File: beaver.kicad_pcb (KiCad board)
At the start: 8 copper layers, 31.2 x 44.5 mm, 57 parts, among them J1 Conn_01x04_Male, J2 USB_C_Receptacle_USB2.0, J3 NFC, J4 Conn_01x17, J5 Conn_01x17, SW1 RESET, SW2 USER P0.17, U1 nRF52840, U2 USBLC6-2SC6, U4 AZ1117-3.3, Y1 Crystal_GND24_Small, Y2 Crystal_Small

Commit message: final touches
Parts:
- added C8: 100n, Capacitor_SMD:C_0402_1005Metric, F.Cu at (162.9, 99.0)
- C5, C6, C7: value 1uF -> 100n
- D2: renamed from D5; value YELLOW P0.24 -> Y P0.10
- D3: renamed from D6; value GREEN P0.22 -> G P1.13
- D4: renamed from D7; value RED P0.20 -> R P1.15
- D5: renamed from D3; value POWER -> PWR
- L1: footprint Inductor_SMD:L_0805_2012Metric -> Inductor_SMD:L_0402_1005Metric
- moved C18 15.1 mm to (172.8, 104.2), turned to 90 degrees
- moved J3 13.9 mm to (170.5, 105.2), turned to -90 degrees
- moved L1 11.6 mm to (169.4, 92.2), turned to 180 degrees
- moved C15 11.3 mm to (169.7, 91.3)
- moved C17 10.9 mm to (165.6, 104.3), turned to -90 degrees
- moved D5 3.52 mm to (156.3, 106.6)
- moved C4 2.28 mm to (163.9, 88.0)
- moved R13 1.59 mm to (153.9, 105.8), turned to 180 degrees
- moved J2 1.41 mm to (174.6, 76.1)
- moved AE1 1.18 mm to (170.3, 76.9)
- moved J1 1.15 mm to (149.2, 76.1)
- moved C1 0.95 mm to (168.4, 94.8)
- moved C24 0.76 mm to (169.6, 108.5)
- moved R8 0.76 mm to (168.6, 108.5)
- moved C21 0.71 mm to (169.7, 87.0)
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- renumbered AE2 to AE1, C15 to C1, C18 to C10, C16 to C11, C19 to C12, C20 to C13, C24 to C14, C1 to C15, C2 to C16, C21 to C17, C22 to C18, C25 to C19, C10 to C2, C26 to C20, C3 to C21, C8 to C22, C4 to C23, C23 to C24, C17 to C3, C11 to C4, C27 to C9, J4 to J1, J5 to J2, J2 to J4, J1 to J5, R15 to R10, R5 to R11, R14 to R12, R7 to R13, R17 to R2, R18 to R3, R19 to R4, R2 to R5, R3 to R6, R6 to R7, R13 to R8, R4 to R9, U4 to U1, U1 to U2, U2 to U3, Y2 to Y1, Y1 to Y2
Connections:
- net Net-(AE2-A) renamed /ANT_MATCHED
- net Net-(J1-Pin_2) renamed /SWDCLK
- net Net-(J1-Pin_3) renamed /SWDIO
- net Net-(U1-ANT) renamed /ANT
- Y2 pad 2: unconnected-(Y1-Pad2) -> GNDREF
- Y2 pad 4: unconnected-(Y1-Pad4) -> GNDREF
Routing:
- net /P0.29: track 0.50 -> 26.6 mm, vias 0 -> 1
- net /SWDCLK: track 0.00 -> 20.5 mm, vias 0 -> 1
- net /SWDIO: track 0.00 -> 20.1 mm, vias 0 -> 1
- net /ANT_MATCHED: track 4.36 -> 15.6 mm
- net /ANT: track 13.8 -> 3.30 mm, vias 2 -> 0
- net /NFC-: track 8.88 -> 18.5 mm
- net VDD: track 58.7 -> 49.4 mm, vias 13 -> 14
- net /NFC+: track 8.67 -> 17.6 mm
- net GNDREF: track 20.6 -> 12.5 mm, vias 11 -> 156
- net /USER_BUT: track 18.3 -> 24.6 mm
- net Net-(U2-DEC2): track 4.96 -> 1.86 mm
- net /P1.12: track 25.2 -> 23.2 mm
- net /P0.26: track 12.5 -> 14.1 mm
- net /P0.31: track 17.4 -> 15.9 mm
- net /P0.25: track 14.4 -> 15.9 mm
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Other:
- board text added: "NFC"
- board text added: "R P1.12 G P0.3 B P0.30"
- board text removed: "B P0.30"
- board text removed: "G P0.3"
- board text removed: "R P1.12"

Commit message: fix: rules due to fabric capabilities
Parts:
- moved J2 1.27 mm to (175.8, 76.1)
- moved J1 1.02 mm to (148.1, 76.1)
- moved C12 0.07 mm to (159.2, 99.0)
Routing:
- net /P1.15: track 21.2 -> 18.2 mm
- net /P1.13: track 15.7 -> 13.2 mm
- net /P0.5: track 13.9 -> 15.9 mm
- net /P0.2: track 16.6 -> 18.0 mm
- net /P1.6: track 20.9 -> 22.2 mm
- net /P1.5: track 19.7 -> 20.9 mm
- net /P0.13: track 18.2 -> 19.2 mm
- net /P0.15: track 23.0 -> 24.0 mm
- net /P0.8: track 13.3 -> 14.3 mm
- net /P0.26: track 14.1 -> 15.1 mm
- net /P0.4: track 11.7 -> 12.7 mm
- net /P0.31: track 15.9 -> 16.7 mm
- net GNDREF: track 12.5 -> 13.3 mm, vias 156 -> 128
- net /P0.12: track 17.3 -> 18.0 mm
- net /DEC_4_6: track 12.6 -> 13.2 mm
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
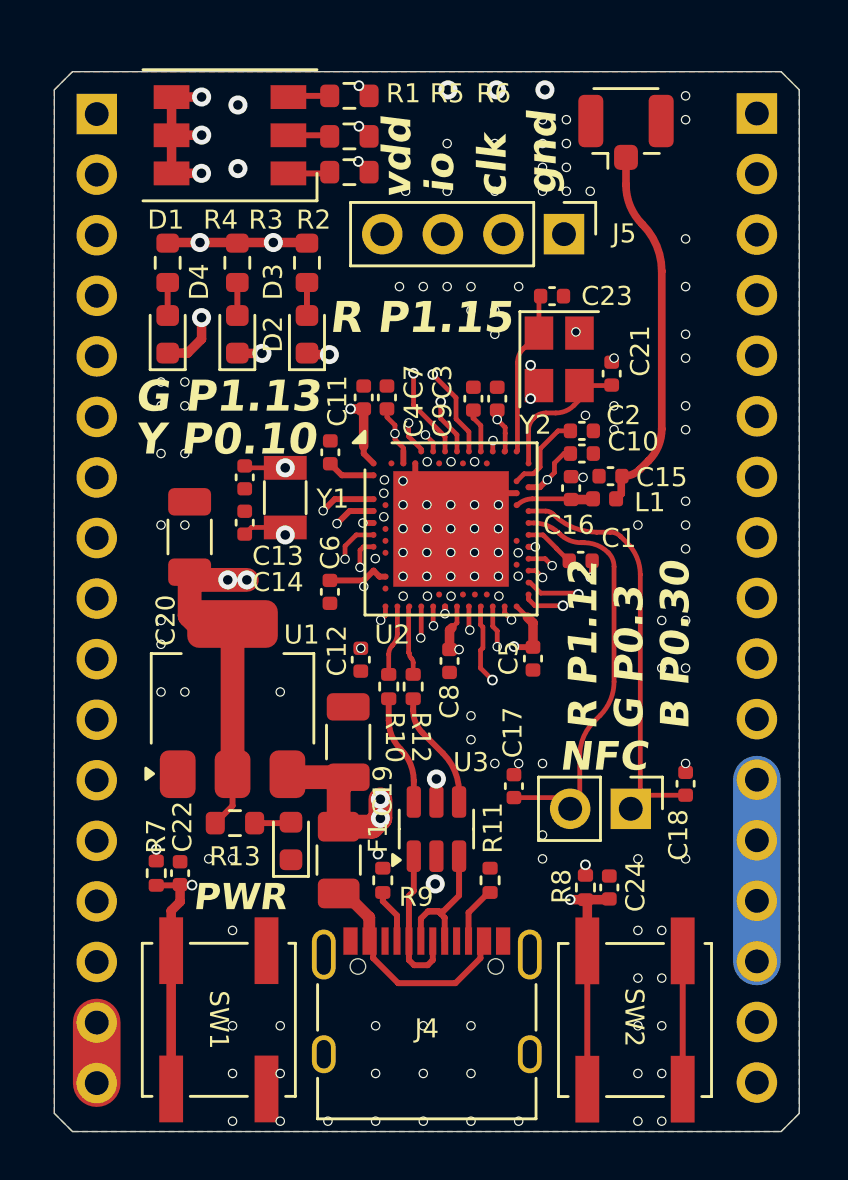
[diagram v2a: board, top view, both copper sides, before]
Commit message: fix: 5V line connection, cat image, text placements, headers edge distanse
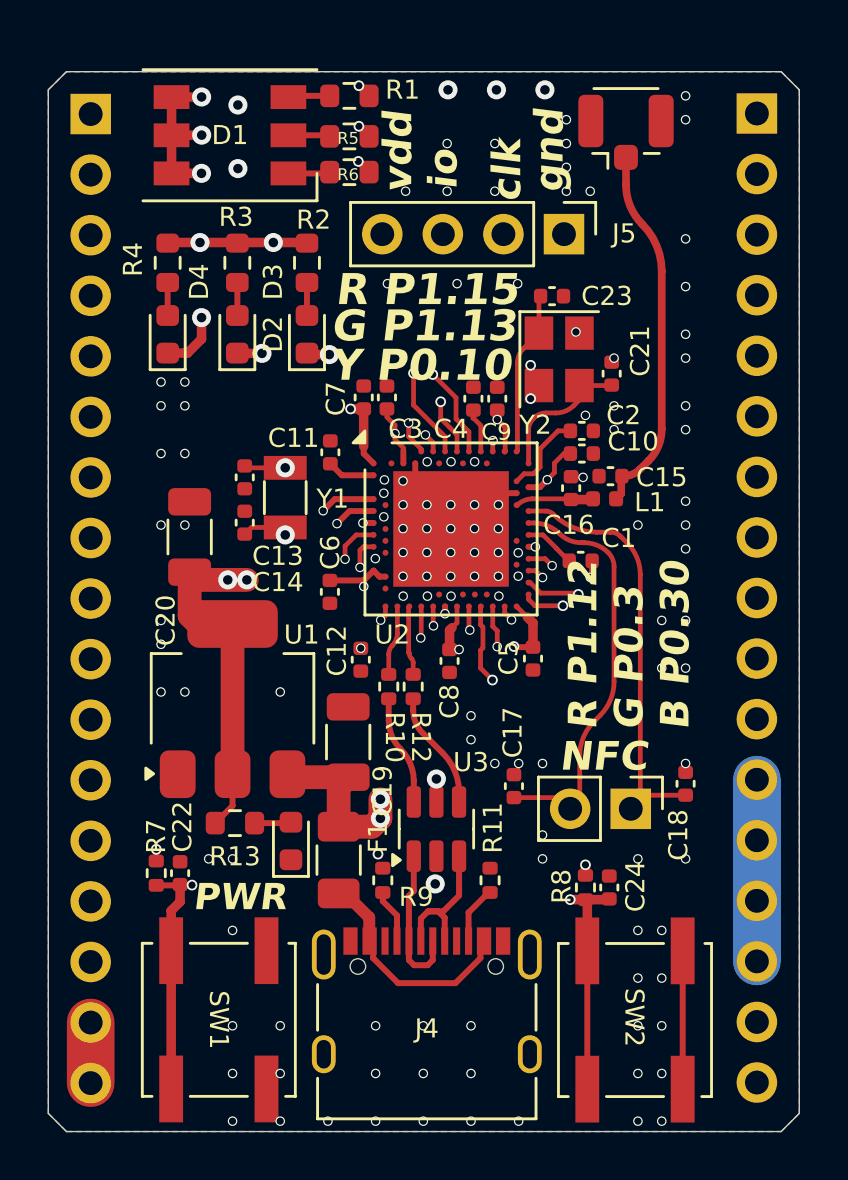
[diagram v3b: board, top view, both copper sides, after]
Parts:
- removed the G*** at (163.4, 96.5)
- added G***: LOGO, Pictures:cat, B.Cu at (167.4, 96.3)
- moved J1 0.25 mm to (147.9, 76.1)
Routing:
- net VBUS: track 41.2 -> 44.1 mm
- net GNDREF: vias 128 -> 119
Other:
- board size 31.2 x 44.5 mm -> 31.5 x 44.5 mm

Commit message: pre-release preparations
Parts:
- added JP1: LDO EN, Connector_PinHeader_2.54mm:PinHeader_1x02_P2.54mm_Vertical, F.Cu at (151.0, 92.1)
- D5: value PWR -> USB IN
- G***: footprint Pictures:cat -> graphics:cat
- Y2: footprint Crystal:Crystal_SMD_3225-4Pin_3.2x2.5mm -> Crystal:Crystal_SMD_2520-4Pin_2.5x2.0mm
- moved D5 2.95 mm to (153.3, 106.6)
- moved R13 1.70 mm to (155.6, 105.9), turned to 0 degrees
- moved C20 1.53 mm to (151.2, 95.1), turned to 180 degrees
- moved G*** 1.12 mm to (168.5, 96.4)
- moved C23 0.42 mm to (167.3, 84.1)
- moved C22 0.40 mm to (151.2, 107.9)
- moved R7 0.40 mm to (150.2, 107.9)
- moved U1 0.32 mm to (153.5, 100.7)
- moved C13 0.28 mm to (154.5, 91.1)
- moved C14 0.28 mm to (154.5, 93.0)
- moved C21 0.25 mm to (169.5, 87.1)
- moved C6 0.23 mm to (158.0, 96.3)
- moved Y1 0.20 mm to (156.2, 92.1)
- moved F1 0.15 mm to (158.4, 107.4)
- moved C4 0.10 mm to (164.0, 88.0)
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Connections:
- C20 pad 1: VDD -> Net-(JP1-A)
- R13 pad 2: VDD -> VBUS
- U1 pad 2: VDD -> Net-(JP1-A)
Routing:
- net VDD: track 48.9 -> 34.7 mm, vias 14 -> 12
- net Net-(JP1-A): track 0.00 -> 12.8 mm
- net /P0.26: track 15.3 -> 13.9 mm
- net /SWDCLK: track 20.1 -> 20.9 mm
- net /P1.5: track 20.9 -> 20.2 mm
- net VBUS: track 44.1 -> 43.5 mm
- net /P0.29: track 26.6 -> 27.3 mm
- net GNDREF: vias 119 -> 140
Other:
- board text added: "USB PWR"
